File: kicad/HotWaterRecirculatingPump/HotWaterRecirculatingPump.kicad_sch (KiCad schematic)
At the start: 12 parts, among them J1 Dual Relay, J2 DS18B20, J3 DS18B20, J4 BUTTON_LED, SW1 SW_WIFI_CONF, U1 DS18B20, U3 mini_esp32

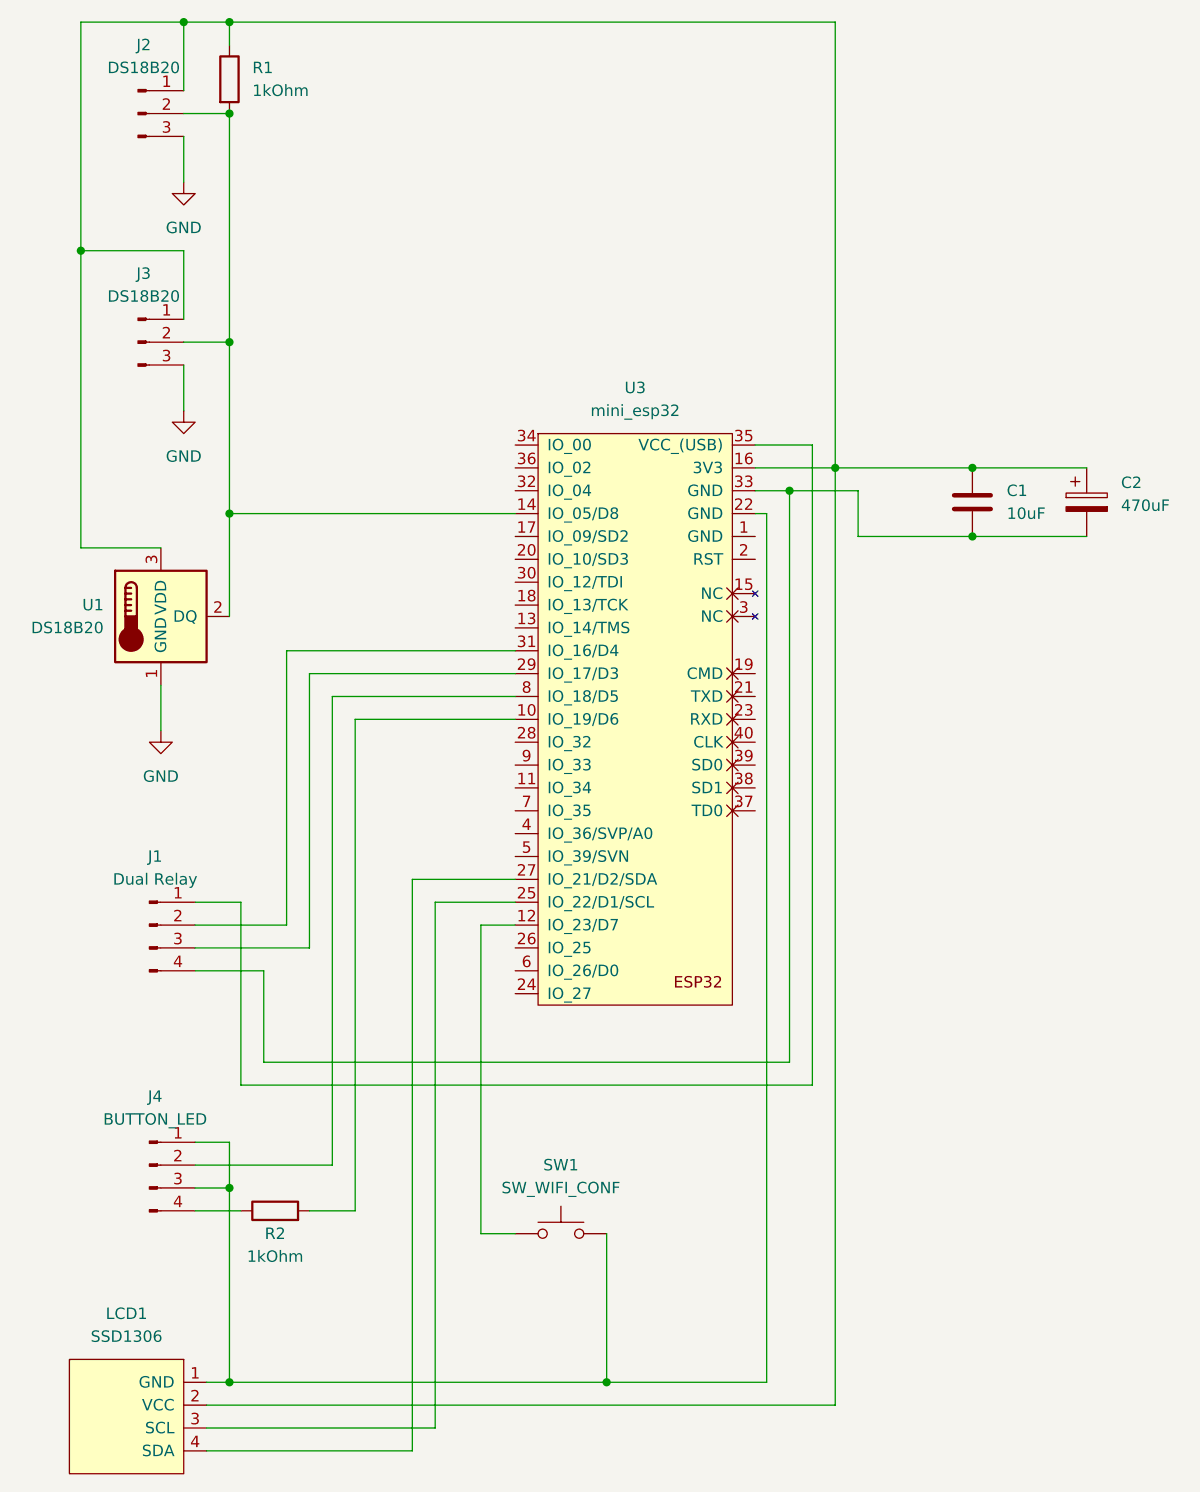
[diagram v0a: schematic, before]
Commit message: Wifi scan working
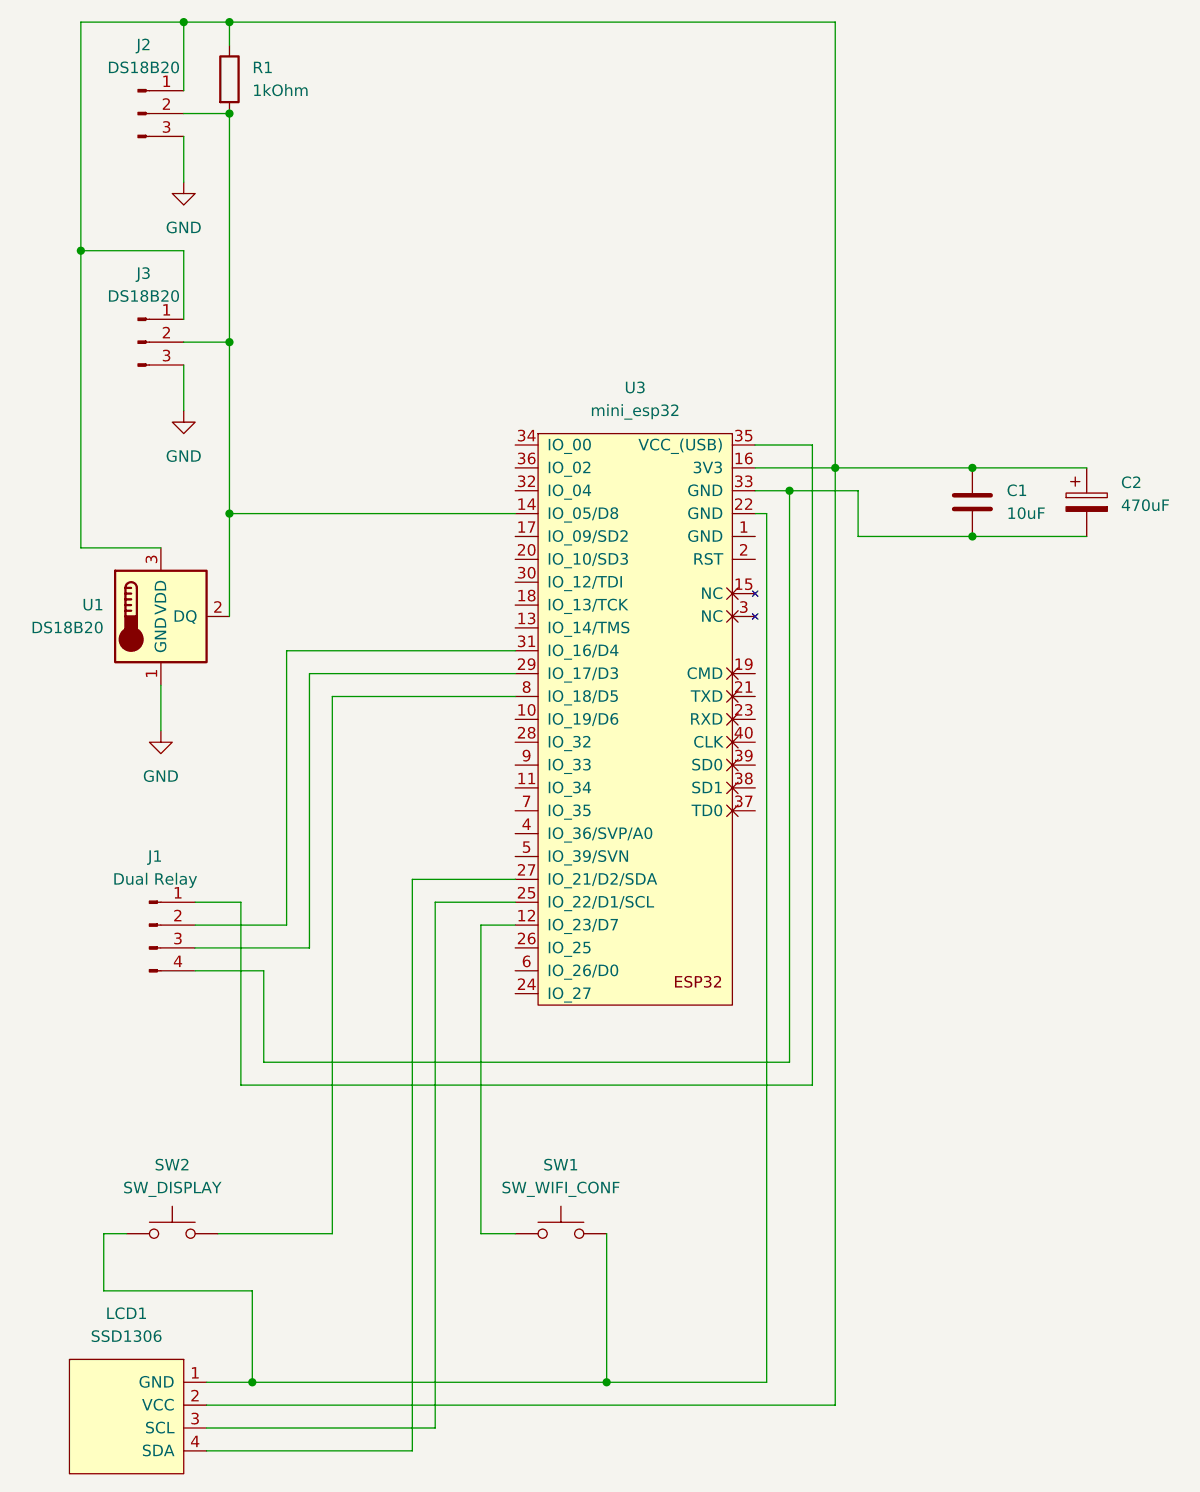
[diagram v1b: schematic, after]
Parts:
- removed J4: BUTTON_LED, Connector_PinHeader_2.54mm:PinHeader_1x04_P2.54mm_Vertical, symbol Connector:Conn_01x04_Male
- removed R2: 1kOhm, Resistor_THT:R_Axial_DIN0207_L6.3mm_D2.5mm_P10.16mm_Horizontal, symbol Device:R
- added SW2: SW_DISPLAY, Button_Switch_THT:SW_PUSH_6mm_H4.3mm, symbol Switch:SW_Push
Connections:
- net at LCD1.1 (GND), SW1.2, U3.22 (GND): now also SW2.1
- net at U3.8 (IO_18/D5): now also SW2.2
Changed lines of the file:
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@@
   (junction (at 86.36 25.4) (diameter 0) (color 0 0 0 0)
   )
-  (junction (at 91.44 176.53) (diameter 0) (color 0 0 0 0)
-  )
-  (junction (at 91.44 154.94) (diameter 0) (color 0 0 0 0)
+  (junction (at 93.98 176.53) (diameter 0) (color 0 0 0 0)
   )
   (wire (pts (xy 161.29 82.55) (xy 161.29 77.47))
     (stroke (width 0) (type default) (color 0 0 0 0))
   )
-  (wire (pts (xy 105.41 102.87) (xy 105.41 157.48))
-    (stroke (width 0) (type default) (color 0 0 0 0))
-  )
   (wire (pts (xy 153.67 77.47) (xy 153.67 140.97))
     (stroke (width 0) (type default) (color 0 0 0 0))
@@
     (stroke (width 0) (type default) (color 0 0 0 0))
   )
-  (wire (pts (xy 91.44 149.86) (xy 91.44 154.94))
-    (stroke (width 0) (type default) (color 0 0 0 0))
-  )
-  (wire (pts (xy 151.13 176.53) (xy 133.35 176.53))
-    (stroke (width 0) (type default) (color 0 0 0 0))
-  )
   (wire (pts (xy 186.69 74.93) (xy 173.99 74.93))
     (stroke (width 0) (type default) (color 0 0 0 0))
@@
     (stroke (width 0) (type default) (color 0 0 0 0))
   )
-  (wire (pts (xy 91.44 176.53) (xy 133.35 176.53))
-    (stroke (width 0) (type default) (color 0 0 0 0))
-  )
-  (wire (pts (xy 123.19 102.87) (xy 105.41 102.87))
+  (wire (pts (xy 93.98 176.53) (xy 133.35 176.53))
     (stroke (width 0) (type default) (color 0 0 0 0))
   )
@@
     (stroke (width 0) (type default) (color 0 0 0 0))
   )
-  (wire (pts (xy 102.87 100.33) (xy 102.87 152.4))
+  (wire (pts (xy 102.87 100.33) (xy 102.87 160.02))
     (stroke (width 0) (type default) (color 0 0 0 0))
   )
@@
     (stroke (width 0) (type default) (color 0 0 0 0))
   )
+  (wire (pts (xy 93.98 166.37) (xy 77.47 166.37))
+    (stroke (width 0) (type default) (color 0 0 0 0))
+  )
   (wire (pts (xy 86.36 43.18) (xy 86.36 38.1))
     (stroke (width 0) (type default) (color 0 0 0 0))
@@
     (stroke (width 0) (type default) (color 0 0 0 0))
   )
-  (wire (pts (xy 87.63 149.86) (xy 91.44 149.86))
-    (stroke (width 0) (type default) (color 0 0 0 0))
-  )
   (wire (pts (xy 74.93 50.8) (xy 74.93 83.82))
     (stroke (width 0) (type default) (color 0 0 0 0))
@@
     (stroke (width 0) (type default) (color 0 0 0 0))
   )
-  (wire (pts (xy 87.63 154.94) (xy 91.44 154.94))
-    (stroke (width 0) (type default) (color 0 0 0 0))
-  )
-  (wire (pts (xy 105.41 157.48) (xy 100.33 157.48))
-    (stroke (width 0) (type default) (color 0 0 0 0))
-  )
-  (wire (pts (xy 92.71 157.48) (xy 87.63 157.48))
+  (wire (pts (xy 77.47 166.37) (xy 77.47 160.02))
     (stroke (width 0) (type default) (color 0 0 0 0))
   )
@@
     (stroke (width 0) (type default) (color 0 0 0 0))
   )
-  (wire (pts (xy 102.87 152.4) (xy 87.63 152.4))
+  (wire (pts (xy 102.87 160.02) (xy 90.17 160.02))
     (stroke (width 0) (type default) (color 0 0 0 0))
   )
@@
     (stroke (width 0) (type default) (color 0 0 0 0))
   )
-  (wire (pts (xy 88.9 176.53) (xy 91.44 176.53))
+  (wire (pts (xy 88.9 176.53) (xy 93.98 176.53))
+    (stroke (width 0) (type default) (color 0 0 0 0))
+  )
+  (wire (pts (xy 133.35 176.53) (xy 151.13 176.53))
     (stroke (width 0) (type default) (color 0 0 0 0))
   )
@@
     (stroke (width 0) (type default) (color 0 0 0 0))
   )
+  (wire (pts (xy 77.47 160.02) (xy 80.01 160.02))
+    (stroke (width 0) (type default) (color 0 0 0 0))
+  )
   (wire (pts (xy 123.19 100.33) (xy 102.87 100.33))
     (stroke (width 0) (type default) (color 0 0 0 0))
@@
     (stroke (width 0) (type default) (color 0 0 0 0))
   )
-  (wire (pts (xy 91.44 154.94) (xy 91.44 176.53))
+  (wire (pts (xy 93.98 166.37) (xy 93.98 176.53))
     (stroke (width 0) (type default) (color 0 0 0 0))
   )
@@
     )
     (property "Datasheet" "~" (id 3) (at 173.99 78.74 0)
-      (effects (font (size 1.27 1.27)) hide)
-    )
-    (pin "1")
-    (pin "2")
-  )
-  (symbol (lib_id "Device:R") (at 96.52 157.48 90) (unit 1)
-    (in_bom yes) (on_board yes)
-    (property "Reference" "R2" (id 0) (at 96.52 160.02 90))
-    (property "Value" "1kOhm" (id 1) (at 96.52 162.56 90))
-    (property "Footprint" "Resistor_THT:R_Axial_DIN0207_L6.3mm_D2.5mm_P10.16mm_Horizontal" (id 2) (at 96.52 159.258 90)
-      (effects (font (size 1.27 1.27)) hide)
-    )
-    (property "Datasheet" "~" (id 3) (at 96.52 157.48 0)
       (effects (font (size 1.27 1.27)) hide)
     )
@@
     (pin "3")
     (pin "4")
+  )
+  (symbol (lib_id "Switch:SW_Push") (at 85.09 160.02 0) (unit 1)
+    (in_bom yes) (on_board yes) (fields_autoplaced)
+    (property "Reference" "SW2" (id 0) (at 85.09 152.4 0))
+    (property "Value" "SW_DISPLAY" (id 1) (at 85.09 154.94 0))
+    (property "Footprint" "Button_Switch_THT:SW_PUSH_6mm_H4.3mm" (id 2) (at 85.09 154.94 0)
+      (effects (font (size 1.27 1.27)) hide)
+    )
+    (property "Datasheet" "~" (id 3) (at 85.09 154.94 0)
+      (effects (font (size 1.27 1.27)) hide)
+    )
+    (pin "1")
+    (pin "2")
   )
   (symbol (lib_id "Connector:Conn_01x03_Male") (at 81.28 35.56 0) (unit 1)
@@
     (pin "3")
   )
-  (symbol (lib_id "Connector:Conn_01x04_Male") (at 82.55 152.4 0) (unit 1)
-    (in_bom yes) (on_board yes)
-    (property "Reference" "J4" (id 0) (at 83.185 144.78 0))
-    (property "Value" "BUTTON_LED" (id 1) (at 83.185 147.32 0))
-    (property "Footprint" "Connector_PinHeader_2.54mm:PinHeader_1x04_P2.54mm_Vertical" (id 2) (at 82.55 152.4 0)
-      (effects (font (size 1.27 1.27)) hide)
-    )
-    (property "Datasheet" "~" (id 3) (at 82.55 152.4 0)
-      (effects (font (size 1.27 1.27)) hide)
-    )
-    (pin "1")
-    (pin "2")
-    (pin "3")
-    (pin "4")
-  )
   (sheet_instances
     (path "/" (page "1"))
@@
       (reference "J3") (unit 1) (value "DS18B20") (footprint "Connector_PinHeader_2.54mm:PinHeader_1x03_P2.54mm_Vertical")
     )
-    (path "/dce56ab1-8dcd-4c40-b0cf-236af78f2702"
-      (reference "J4") (unit 1) (value "BUTTON_LED") (footprint "Connector_PinHeader_2.54mm:PinHeader_1x04_P2.54mm_Vertical")
-    )
     (path "/6357f211-c625-4583-8d03-d7f8a4300c37"
       (reference "LCD1") (unit 1) (value "SSD1306") (footprint "SSD1306:128x64OLED")
@@
       (reference "R1") (unit 1) (value "1kOhm") (footprint "Resistor_THT:R_Axial_DIN0207_L6.3mm_D2.5mm_P10.16mm_Horizontal")
     )
-    (path "/501e5c45-1f09-4858-8280-e30bbc1e6cff"
-      (reference "R2") (unit 1) (value "1kOhm") (footprint "Resistor_THT:R_Axial_DIN0207_L6.3mm_D2.5mm_P10.16mm_Horizontal")
-    )
     (path "/194a7bc0-9afd-48ad-8c20-8d5582779a92"
       (reference "SW1") (unit 1) (value "SW_WIFI_CONF") (footprint "Button_Switch_THT:SW_PUSH_6mm_H4.3mm")
     )
+    (path "/6f41e1f9-f264-42ca-8dba-1d7984e08d0f"
+      (reference "SW2") (unit 1) (value "SW_DISPLAY") (footprint "Button_Switch_THT:SW_PUSH_6mm_H4.3mm")
+    )
     (path "/c8bf974c-c44e-4d6d-886d-389cb6869973"
